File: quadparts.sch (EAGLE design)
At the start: 69 parts, among them J1 AVR_SPI_PRG_6NS, U1 ATMEGA128RFA1, Y1 16MHz

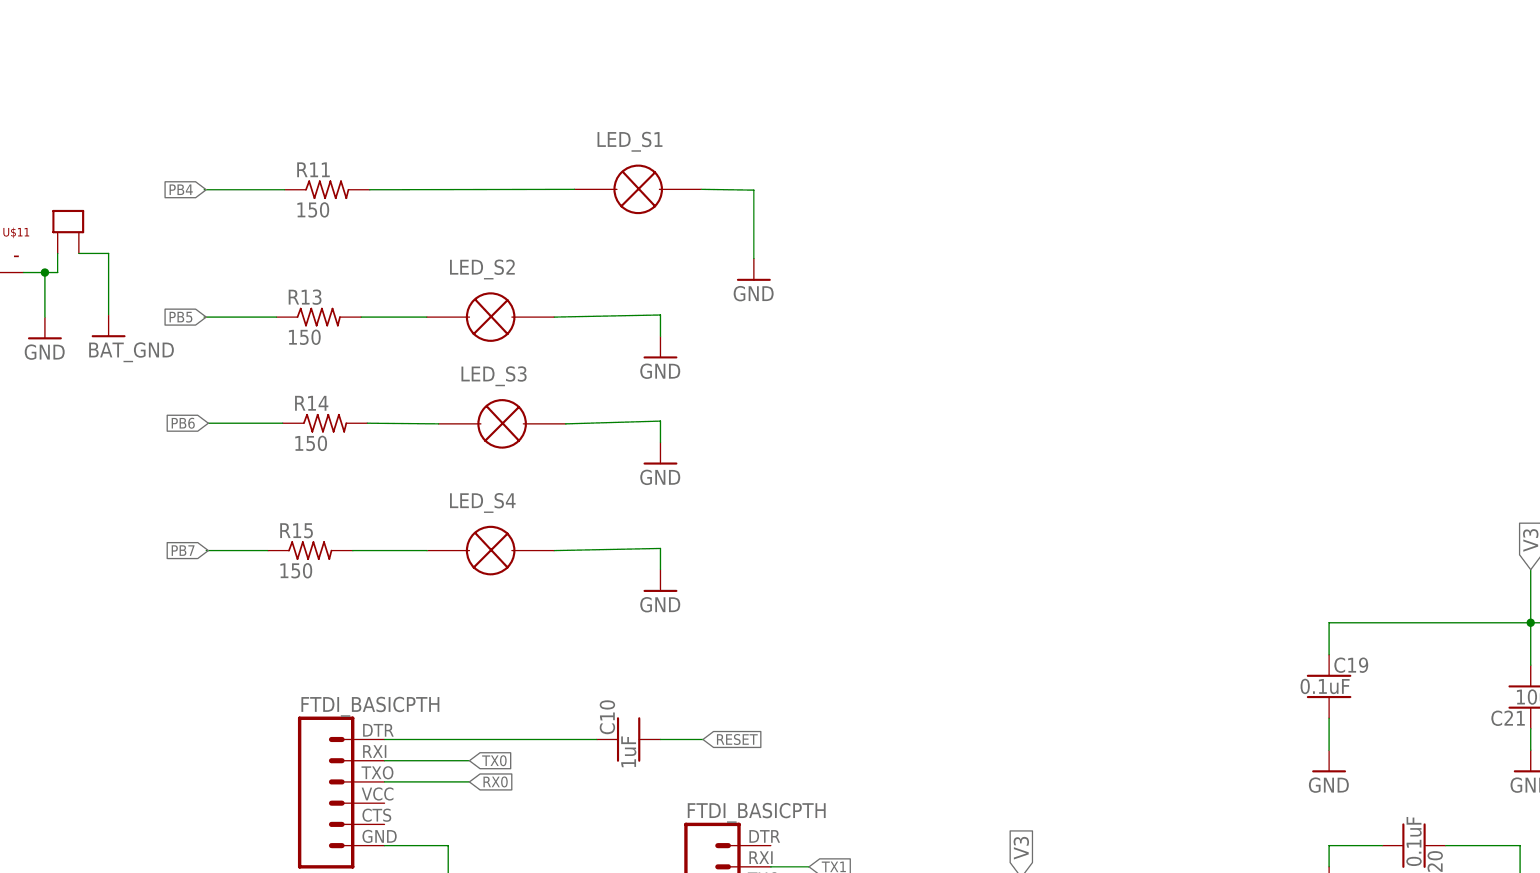
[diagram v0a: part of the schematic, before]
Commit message: ... Zhe help I'm not sure how to fix the board
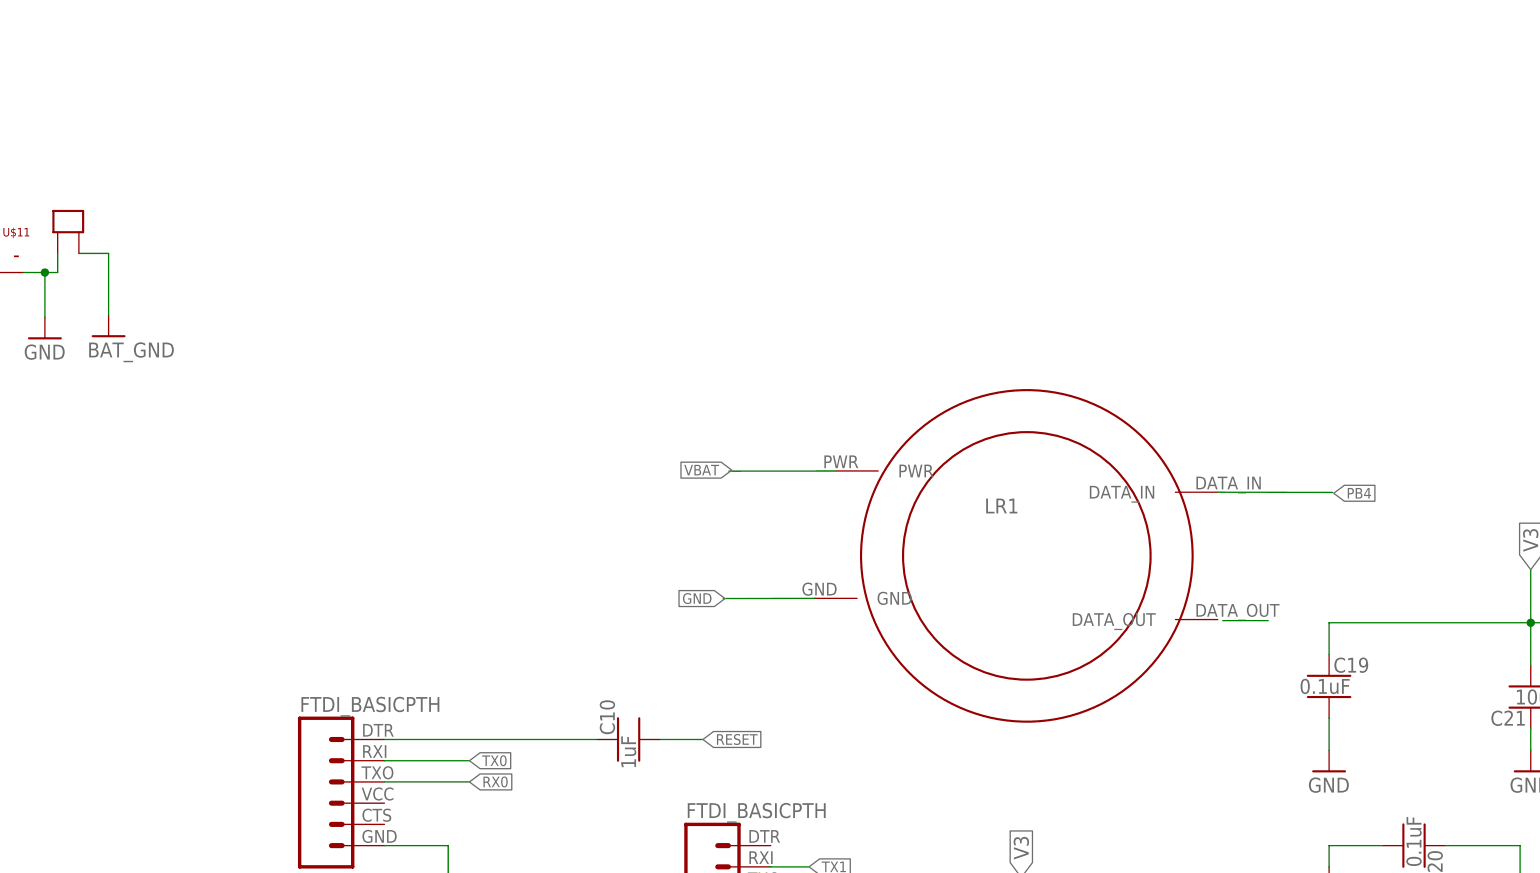
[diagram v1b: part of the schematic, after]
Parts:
- removed LED_S1, LED_S2, LED_S3, LED_S4: (no value), LEDs:LED
- removed R11, R13, R14, R15: 150, quadparts_prebuilt:RESISTOR_SMD-2012-0805-100
- added LR1: LED_RING, LEDs:LED_RING
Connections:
- removed net N$5: LED_S1.P$1, R11.2
- removed net N$6: LED_S2.P$1, R13.2
- removed net N$7: LED_S3.P$1, R14.2
- removed net N$9: LED_S4.P$1, R15.2
- net GND: now also LR1.GND; no longer LED_S1.P$2, LED_S2.P$2, LED_S3.P$2, LED_S4.P$2
- net PB4: now also LR1.DATA_IN; no longer R11.1
- net PB5: no longer R13.1
- net PB6: no longer R14.1
- net PB7: no longer R15.1
- net VBAT: now also LR1.PWR
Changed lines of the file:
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@@
 <part name="GND37" library="quadparts_prebuilt" deviceset="GND" device=""/>
 <part name="GND38" library="quadparts_prebuilt" deviceset="BAT_GND" device=""/>
-<part name="GND39" library="quadparts_prebuilt" deviceset="GND" device=""/>
-<part name="GND40" library="quadparts_prebuilt" deviceset="GND" device=""/>
-<part name="GND41" library="quadparts_prebuilt" deviceset="GND" device=""/>
-<part name="GND42" library="quadparts_prebuilt" deviceset="GND" device=""/>
 <part name="C5" library="quadparts_prebuilt" deviceset="CAPACITOR-NP_" device="SMD-2012-0805_CERAMIC-1UF" value="1uF"/>
 <part name="C6" library="quadparts_prebuilt" deviceset="CAPACITOR-NP_" device="SMD-2012-0805_CERAMIC-1UF" value="1uF"/>
@@
 <part name="C28" library="quadparts_prebuilt" deviceset="CAPACITOR-NP_" device="SMD-2012-0805_CERAMIC-1UF" value="1uF"/>
 <part name="C29" library="quadparts_prebuilt" deviceset="CAPACITOR-NP_" device="SMD-2012-0805_CERAMIC-1UF" value="1uF"/>
-<part name="LED_S1" library="LEDs" deviceset="LED" device=""/>
-<part name="LED_S2" library="LEDs" deviceset="LED" device=""/>
-<part name="LED_S3" library="LEDs" deviceset="LED" device=""/>
-<part name="LED_S4" library="LEDs" deviceset="LED" device=""/>
 <part name="J2" library="quadparts_Jason" deviceset="MALE_HEADER_2POS" device="-2X1-0.1IN"/>
 <part name="D1" library="quadparts_prebuilt" deviceset="DIODE-SCHOTTKY_" device="SMD-SOD123-360MV" value="360mV"/>
@@
 <part name="GND24" library="quadparts_prebuilt" deviceset="BAT_GND" device=""/>
 <part name="GND26" library="quadparts_prebuilt" deviceset="BAT_GND" device=""/>
-<part name="R11" library="quadparts_prebuilt" deviceset="RESISTOR_" device="SMD-2012-0805-100" value="150"/>
-<part name="R13" library="quadparts_prebuilt" deviceset="RESISTOR_" device="SMD-2012-0805-100" value="150"/>
-<part name="R14" library="quadparts_prebuilt" deviceset="RESISTOR_" device="SMD-2012-0805-100" value="150"/>
-<part name="R15" library="quadparts_prebuilt" deviceset="RESISTOR_" device="SMD-2012-0805-100" value="150"/>
 <part name="R2" library="quadparts_prebuilt" deviceset="RESISTOR_" device="SMD-2012-0805-10K" value="10K"/>
 <part name="R3" library="quadparts_prebuilt" deviceset="RESISTOR_" device="SMD-2012-0805-10K" value="10K"/>
@@
 <part name="C3" library="quadparts_prebuilt" deviceset="CAPACITOR-NP_" device="SMD-2012-0805_CERAMIC-0.1UF" value="0.1uF"/>
 <part name="C4" library="quadparts_prebuilt" deviceset="CAPACITOR-NP_" device="SMD-2012-0805_CERAMIC-0.1UF" value="0.1uF"/>
+<part name="LR1" library="LEDs" deviceset="LED_RING" device=""/>
 </parts>
 <sheets>
@@
 <instance part="GND37" gate="1" x="-15.24" y="200.66"/>
 <instance part="GND38" gate="1" x="88.9" y="200.66"/>
-<instance part="GND39" gate="1" x="166.116" y="207.404"/>
-<instance part="GND40" gate="1" x="154.94" y="198.12"/>
-<instance part="GND41" gate="1" x="154.94" y="185.42"/>
-<instance part="GND42" gate="1" x="154.94" y="170.18"/>
 <instance part="C5" gate="G$1" x="38.1" y="114.3" rot="R180"/>
 <instance part="C6" gate="G$1" x="48.26" y="114.3" rot="R180"/>
@@
 <instance part="C28" gate="G$1" x="96.52" y="33.02"/>
 <instance part="C29" gate="G$1" x="104.14" y="33.02"/>
-<instance part="LED_S1" gate="G$1" x="152.274" y="218.232"/>
-<instance part="LED_S2" gate="G$1" x="134.62" y="202.946"/>
-<instance part="LED_S3" gate="G$1" x="135.9916" y="190.1698"/>
-<instance part="LED_S4" gate="G$1" x="134.62" y="175.006"/>
 <instance part="J2" gate="G$1" x="43.18" y="205.74" rot="R270"/>
 <instance part="D1" gate="G$1" x="224.79" y="17.78" rot="R90"/>
@@
 <instance part="GND24" gate="1" x="261.62" y="-41.148"/>
 <instance part="GND26" gate="1" x="337.82" y="-41.402"/>
-<instance part="R11" gate="G$1" x="115.062" y="218.186"/>
-<instance part="R13" gate="G$1" x="114.046" y="202.946"/>
-<instance part="R14" gate="G$1" x="114.808" y="190.246"/>
-<instance part="R15" gate="G$1" x="113.03" y="175.006"/>
 <instance part="R2" gate="G$1" x="218.487" y="121.36" rot="R270"/>
 <instance part="R3" gate="G$1" x="212.3402" y="121.106" rot="R270"/>
@@
 <instance part="C3" gate="G$1" x="264.16" y="-22.352"/>
 <instance part="C4" gate="G$1" x="340.36" y="-19.812"/>
+<instance part="LR1" gate="G$1" x="198.7804" y="174.371"/>
 </instances>
 <busses>
@@
 </segment>
 <segment>
-<pinref part="R11" gate="G$1" pin="1"/>
-<wire x1="109.982" y1="218.186" x2="100.33" y2="218.186" width="0.1524" layer="91"/>
-<label x="100.584" y="218.186" size="1.27" layer="95" rot="R180" xref="yes"/>
+<pinref part="LR1" gate="G$1" pin="DATA_IN"/>
+<wire x1="221.6404" y1="181.991" x2="235.3818" y2="181.9656" width="0.1524" layer="91"/>
+<label x="235.5088" y="181.864" size="1.27" layer="95" xref="yes"/>
 </segment>
 </net>
@@
 </segment>
 <segment>
-<pinref part="R13" gate="G$1" pin="1"/>
-<wire x1="108.966" y1="202.946" x2="100.33" y2="202.946" width="0.1524" layer="91"/>
-<label x="100.584" y="202.946" size="1.27" layer="95" rot="R180" xref="yes"/>
-</segment>
-<segment>
 <wire x1="90.1192" y1="-4.7244" x2="94.234" y2="-4.699" width="0.1524" layer="91"/>
 <pinref part="R12" gate="G$1" pin="1"/>
@@
 <label x="5.08" y="81.28" size="1.27" layer="95" rot="R180" xref="yes"/>
 </segment>
-<segment>
-<pinref part="R14" gate="G$1" pin="1"/>
-<wire x1="109.728" y1="190.246" x2="100.838" y2="190.246" width="0.1524" layer="91"/>
-<label x="100.838" y="190.246" size="1.27" layer="95" rot="R180" xref="yes"/>
-</segment>
 </net>
 <net name="PB7" class="0">
@@
 <wire x1="12.7" y1="78.74" x2="5.08" y2="78.74" width="0.1524" layer="91"/>
 <label x="5.08" y="78.74" size="1.27" layer="95" rot="R180" xref="yes"/>
-</segment>
-<segment>
-<pinref part="R15" gate="G$1" pin="1"/>
-<wire x1="107.95" y1="175.006" x2="100.584" y2="175.006" width="0.1524" layer="91"/>
-<label x="100.838" y="175.006" size="1.27" layer="95" rot="R180" xref="yes"/>
 </segment>
 </net>
@@
 </segment>
 <segment>
-<pinref part="GND41" gate="1" pin="GND"/>
-<wire x1="143.6116" y1="190.1698" x2="154.94" y2="190.5" width="0.1524" layer="91"/>
-<wire x1="154.94" y1="190.5" x2="154.94" y2="187.96" width="0.1524" layer="91"/>
-<pinref part="LED_S3" gate="G$1" pin="P$2"/>
-</segment>
-<segment>
-<pinref part="GND42" gate="1" pin="GND"/>
-<wire x1="142.24" y1="175.006" x2="154.94" y2="175.26" width="0.1524" layer="91"/>
-<wire x1="154.94" y1="175.26" x2="154.94" y2="172.72" width="0.1524" layer="91"/>
-<pinref part="LED_S4" gate="G$1" pin="P$2"/>
-</segment>
-<segment>
 <pinref part="U1" gate="G$1" pin="PG4(TOSC1)"/>
 <wire x1="12.7" y1="17.78" x2="-2.54" y2="17.78" width="0.1524" layer="91"/>
@@
 <wire x1="68.58" y1="17.78" x2="68.58" y2="5.08" width="0.1524" layer="91"/>
 <pinref part="GND8" gate="1" pin="GND"/>
-</segment>
-<segment>
-<pinref part="LED_S2" gate="G$1" pin="P$2"/>
-<pinref part="GND40" gate="1" pin="GND"/>
-<wire x1="142.24" y1="202.946" x2="154.94" y2="203.2" width="0.1524" layer="91"/>
-<wire x1="154.94" y1="203.2" x2="154.94" y2="200.66" width="0.1524" layer="91"/>
-</segment>
-<segment>
-<pinref part="LED_S1" gate="G$1" pin="P$2"/>
-<pinref part="GND39" gate="1" pin="GND"/>
-<wire x1="159.894" y1="218.232" x2="166.116" y2="218.14" width="0.1524" layer="91"/>
-<wire x1="166.116" y1="218.14" x2="166.116" y2="209.944" width="0.1524" layer="91"/>
 </segment>
 <segment>
@@
 <wire x1="168.148" y1="127" x2="174.244" y2="127" width="0.1524" layer="91"/>
 <wire x1="174.244" y1="127" x2="174.244" y2="121.158" width="0.1524" layer="91"/>
+</segment>
+<segment>
+<pinref part="LR1" gate="G$1" pin="GND"/>
+<wire x1="173.3804" y1="169.291" x2="162.433" y2="169.2656" width="0.1524" layer="91"/>
+<label x="162.6616" y="169.2656" size="1.27" layer="95" rot="R180" xref="yes"/>
 </segment>
 </net>
@@
 <wire x1="304.8" y1="18.542" x2="304.8" y2="21.59" width="0.1524" layer="91"/>
 <junction x="271.78" y="21.59"/>
+</segment>
+<segment>
+<pinref part="LR1" gate="G$1" pin="PWR"/>
+<wire x1="175.9204" y1="184.531" x2="163.1188" y2="184.5056" width="0.1524" layer="91"/>
+<label x="163.4744" y="184.6326" size="1.27" layer="95" rot="R180" xref="yes"/>
 </segment>
 </net>
@@
 </segment>
 </net>
-<net name="N$5" class="0">
-<segment>
-<pinref part="R11" gate="G$1" pin="2"/>
-<pinref part="LED_S1" gate="G$1" pin="P$1"/>
-<wire x1="120.142" y1="218.186" x2="144.654" y2="218.232" width="0.1524" layer="91"/>
-</segment>
-</net>
-<net name="N$6" class="0">
-<segment>
-<pinref part="R13" gate="G$1" pin="2"/>
-<pinref part="LED_S2" gate="G$1" pin="P$1"/>
-<wire x1="119.126" y1="202.946" x2="127" y2="202.946" width="0.1524" layer="91"/>
-</segment>
-</net>
-<net name="N$7" class="0">
-<segment>
-<pinref part="R14" gate="G$1" pin="2"/>
-<pinref part="LED_S3" gate="G$1" pin="P$1"/>
-<wire x1="119.888" y1="190.246" x2="128.3716" y2="190.1698" width="0.1524" layer="91"/>
-</segment>
-</net>
-<net name="N$9" class="0">
-<segment>
-<pinref part="R15" gate="G$1" pin="2"/>
-<pinref part="LED_S4" gate="G$1" pin="P$1"/>
-<wire x1="118.11" y1="175.006" x2="127" y2="175.006" width="0.1524" layer="91"/>
-</segment>
-</net>
 <net name="N$2" class="0">
 <segment>
@@
 </segment>
 </net>
+<net name="N$7" class="0">
+<segment>
+<wire x1="222.2246" y1="166.624" x2="227.6602" y2="166.624" width="0.1524" layer="91"/>
+</segment>
+</net>

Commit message: fix everything
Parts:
- removed C1, C2, C3, C4: 0.1uF, quadparts_prebuilt:CAPACITOR-NP_SMD-2012-0805_CERAMIC-0.1UF
- added C13, C15, C7, C9: 0.1uF, quadparts_Jason:CERAMIC_CAP-0805-0.1UF
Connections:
- removed net N$11: C4.1, R10.2, R9.2, U$9.G
- removed net N$12: C1.1, R12.2, R5.2, U$2.G
- removed net N$3: C3.1, R7.2, R8.2, U$7.G
- new net N$14: C13.1, R7.2, R8.2, U$7.G
- new net N$18: C15.1, R10.2, R9.2, U$9.G
- net BAT_GND: now also C13.2, C15.2, C7.2, C9.2; no longer C1.2, C2.2, C3.2, C4.2
- net GND: no longer JP2.6
- net N$2: now also C7.1; no longer C2.1
- net PB5: now also C9.1, R12.2, R5.2, U$2.G
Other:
- moved on the sheet: C25, JP2, LR1, R12, R7

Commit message: minor fix the board
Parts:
- BREAKOUT_HEADER: value (none) -> NOVALUE
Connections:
- removed net A0: U1.PF0(ADC0)
- removed net A1: U1.PF1(ADC1)
- removed net A2: U1.PF2(ADC2/DIG2)
- removed net A3: U1.PF3(ADC3/DIG4)
- removed net A4: U1.PF4(ADC4/TCK)
- removed net A5: U1.PF5(ADC5/TMS)
- removed net A6: U1.PF6(ADC6/TDO)
- removed net A7: U1.PF7(ADC7/TDI)
- removed net AREF: U1.AREF
- removed net PB6: U1.PB6(OC1B/PCINT6)
- removed net PB7: U1.PB7(OC0A/OC1C/PCINT7)
- removed net PD4: U1.PD4(ICP1)
- removed net PD5: U1.PD5(XCK1)
- removed net PD6: U1.PD6(T1)
- removed net PD7: U1.PD7(T0)
- removed net PE2: U1.PE2(XCK0/AIN0)
- removed net PE6: U1.PE6(T3/INT6)
- removed net PE7: U1.PE7(ICP3/INT7/CLKO)
- removed net PG0: U1.PG0(DIG3)
- removed net PG1: U1.PG1(DIG1)
- removed net PG2: U1.PG2(AMR)
- removed net PG5: U1.PG5(OC0B)
- removed net RSTON: U1.RSTON
- removed net SSN: U1.PB0(SSN/PCINT0)
- new net N$1: C9.1, R12.2, R5.2, U$2.G
- net PB5: no longer C9.1, R12.2, R5.2, U$2.G
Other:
- moved on the sheet: C9, R12
